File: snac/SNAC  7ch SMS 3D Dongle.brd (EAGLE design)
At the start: 37.2 x 21.9 mm, 11 parts, among them IC1 4030D, K2 692112030100, Q9 BC849SMD, X2 STEREOJACK

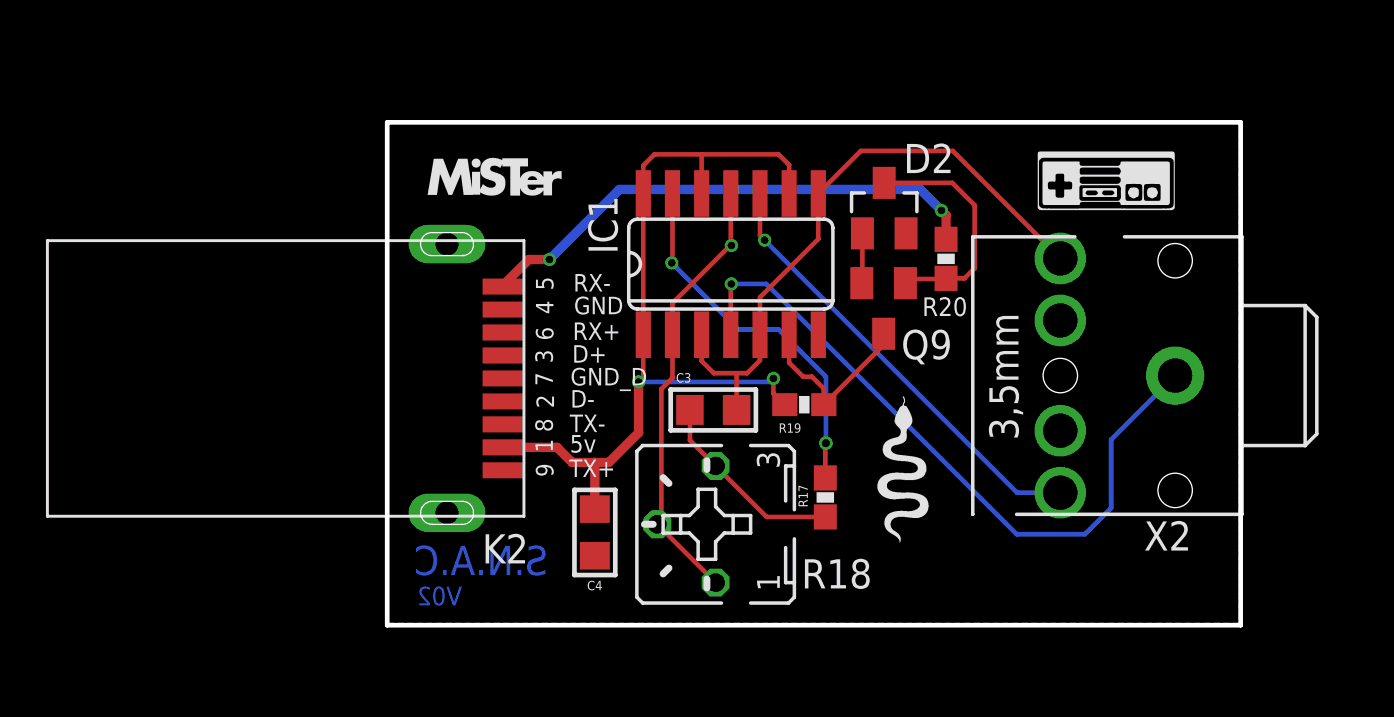
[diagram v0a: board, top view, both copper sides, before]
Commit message: Added charge pump to the SMS 3D and SMS DB9 3D PCBs
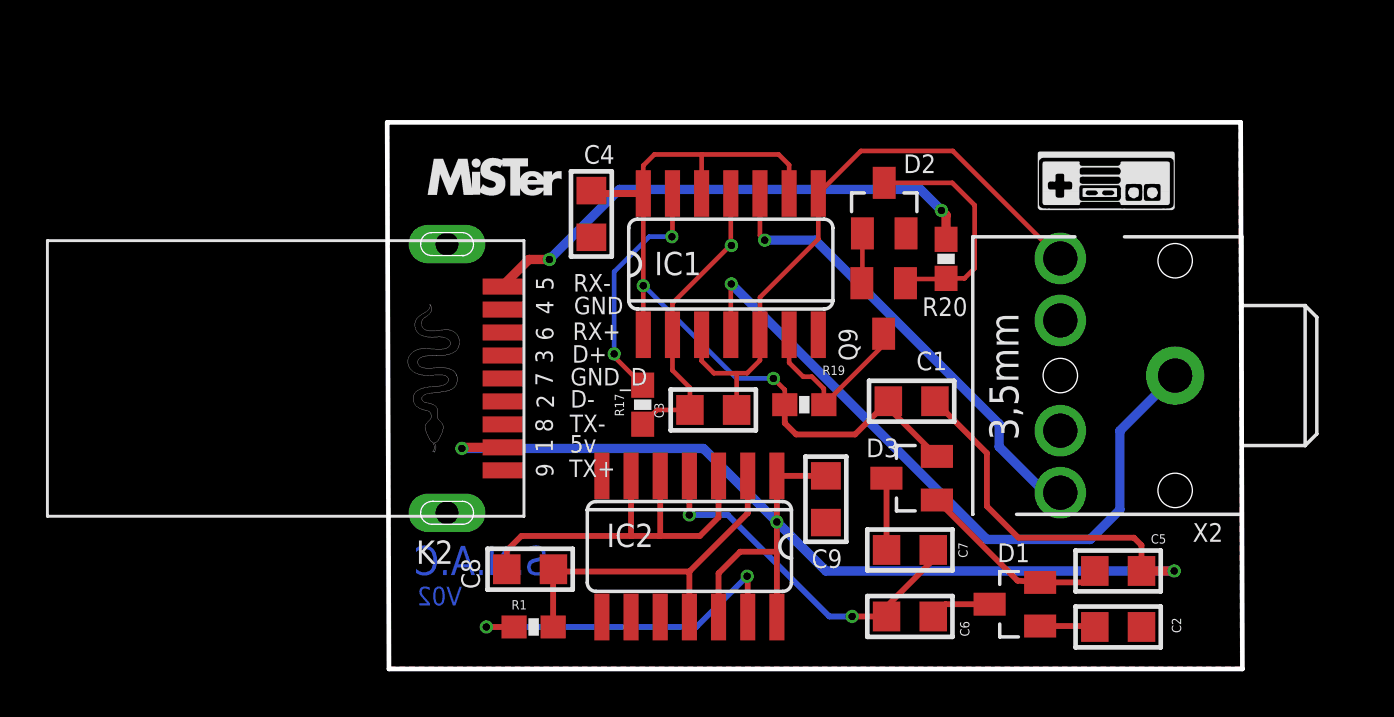
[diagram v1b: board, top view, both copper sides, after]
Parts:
- removed R18: 47K, pot:B25P
- added C1, C2, C5, C6, C7: 2.2uF, rc-master-smd:C0805
- added C8: 10nF, rc-master-smd:C0805
- added C9: 22uF, rc-master-smd:C0805
- added D1, D3: BAS40-04, diode:SOT23
- added IC2: 4030D, 40xx:SO14
- added R1: 75K, SparkFun:0603-RES
- R17: value 22K -> 75K
- moved C4 13.9 mm to (8.92, 17.8)
- moved R17 8.92 mm to (11.2, 9.53), turned to 270 degrees
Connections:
- new net 10V: C1.1, C4.1, D3.2, IC1.1, IC1.12, IC1.14, IC1.9, R19.1
- new net N$11: C7.2, D3.3
- new net N$12: C6.2, D1.3
- new net N$16: C8.1, IC2.11, IC2.2, R1.2
- new net N$17: IC2.13, R1.1
- new net N$6: C5.1, D1.2, D3.1
- new net N$7: C6.1, C7.1, IC2.4
- new net N$8: C2.1, D1.1
- net GND: now also C2.2, C9.2, IC2.7, IC2.8, IC2.9
- net HV: now also C1.2, C5.2, C9.1, IC2.1, IC2.12, IC2.14; no longer C4.1, IC1.1, IC1.12, IC1.14, IC1.9, R19.1
- net N$10: now also R17.1; no longer R17.2
- net N$5: now also C3.1, R17.2; no longer R18.A, R18.S
- net N$9: now also C8.2, IC2.3, IC2.5, IC2.6; no longer C3.1, R17.1, R18.E
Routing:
- net 10V: track 0.00 -> 37.5 mm, vias 0 -> 2
- net HV: track 37.6 -> 63.6 mm, vias 2 -> 3
- net N$7: track 0.00 -> 15.9 mm, vias 0 -> 2
- net N$16: track 0.00 -> 15.7 mm
- net N$17: track 0.00 -> 15.3 mm, vias 0 -> 2
- net N$9: track 8.60 -> 17.7 mm
- net N$6: track 0.00 -> 8.54 mm
- net N$5: track 19.4 -> 13.2 mm
- net N$10: track 16.2 -> 10.5 mm
- net N$11: track 0.00 -> 3.13 mm
- net N$12: track 0.00 -> 2.68 mm
- net N$8: track 0.00 -> 2.40 mm
- net RING: track 19.5 -> 20.1 mm
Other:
- board size 37.2 x 21.9 mm -> 37.2 x 23.8 mm

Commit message: Updated PCB images and README
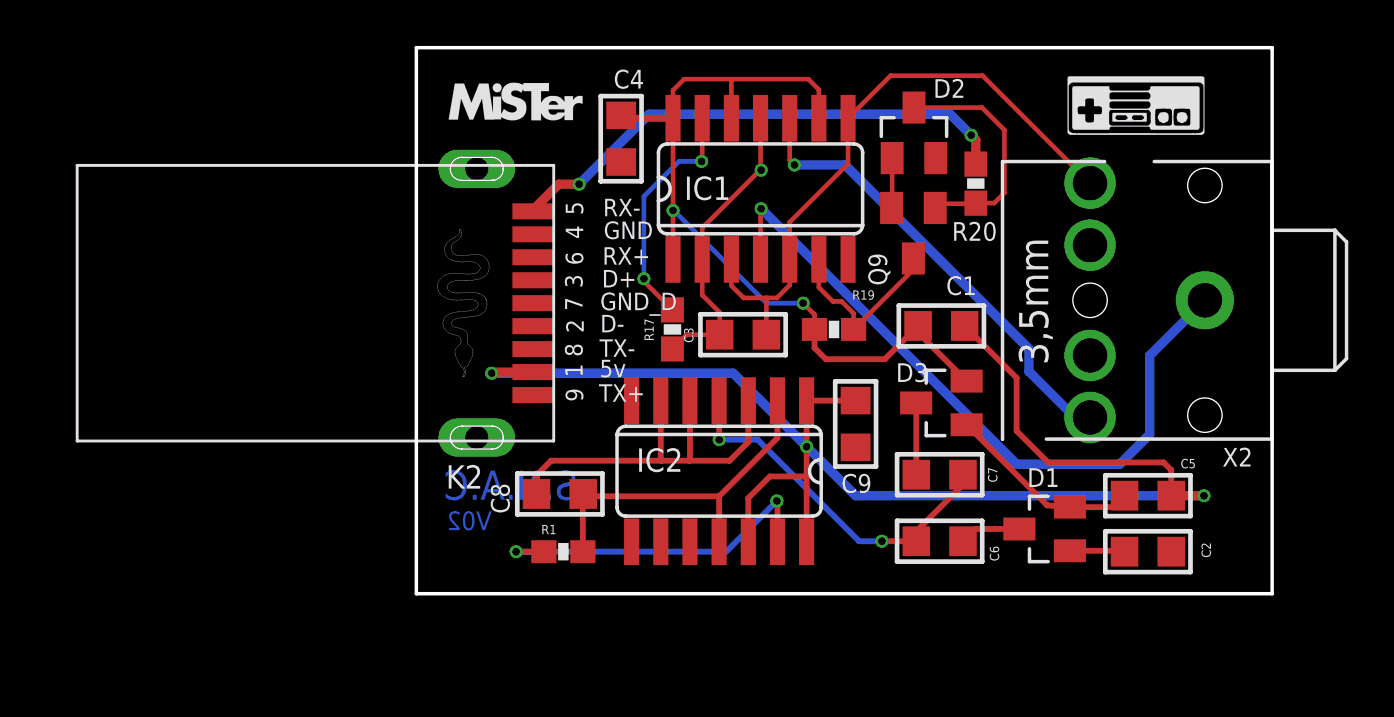
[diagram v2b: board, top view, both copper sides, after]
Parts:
- moved C1 3.52 mm to (24.2, 13.0)
- moved C7 3.52 mm to (24.1, 6.48)
- moved C9 3.52 mm to (20.4, 8.69)
- moved D3 3.52 mm to (24.2, 9.60)
- moved Q9 3.52 mm to (22.9, 17.0)
- moved R19 3.52 mm to (19.5, 12.8)
- moved X2 3.52 mm to (38.3, 14.0)
- moved C3 3.52 mm to (15.5, 12.6)
- moved C6 3.52 mm to (24.1, 3.58)
- moved D1 3.52 mm to (28.7, 4.11)
- moved K2 3.52 mm to (6.38, 13.9)
- moved R1 3.52 mm to (7.70, 3.12)
- moved R17 3.52 mm to (12.4, 12.8)
- moved C8 3.52 mm to (7.54, 5.64)
- moved IC2 3.52 mm to (14.5, 6.63)
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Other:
- board size 37.2 x 23.8 mm -> 37.3 x 23.8 mm
- board text removed: "+"
- board text removed: "-"
